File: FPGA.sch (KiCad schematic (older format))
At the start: 1 part, among them U300 LFE5U-12F-8BG256C

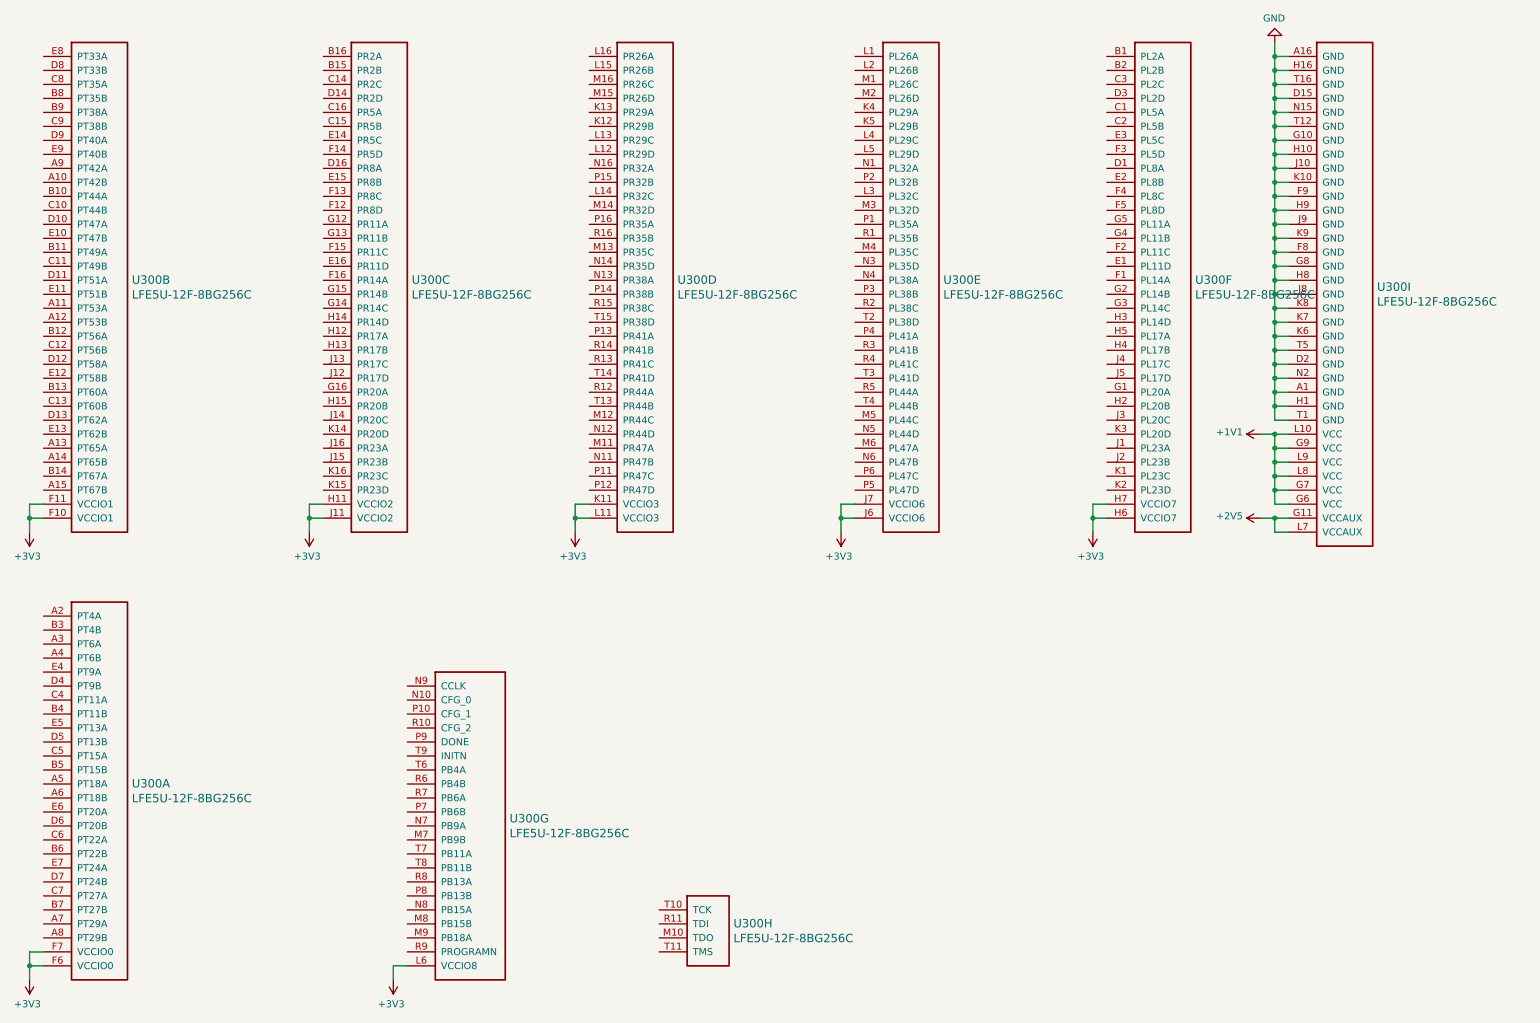
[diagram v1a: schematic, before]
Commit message: updated schematic and initial bga fanout
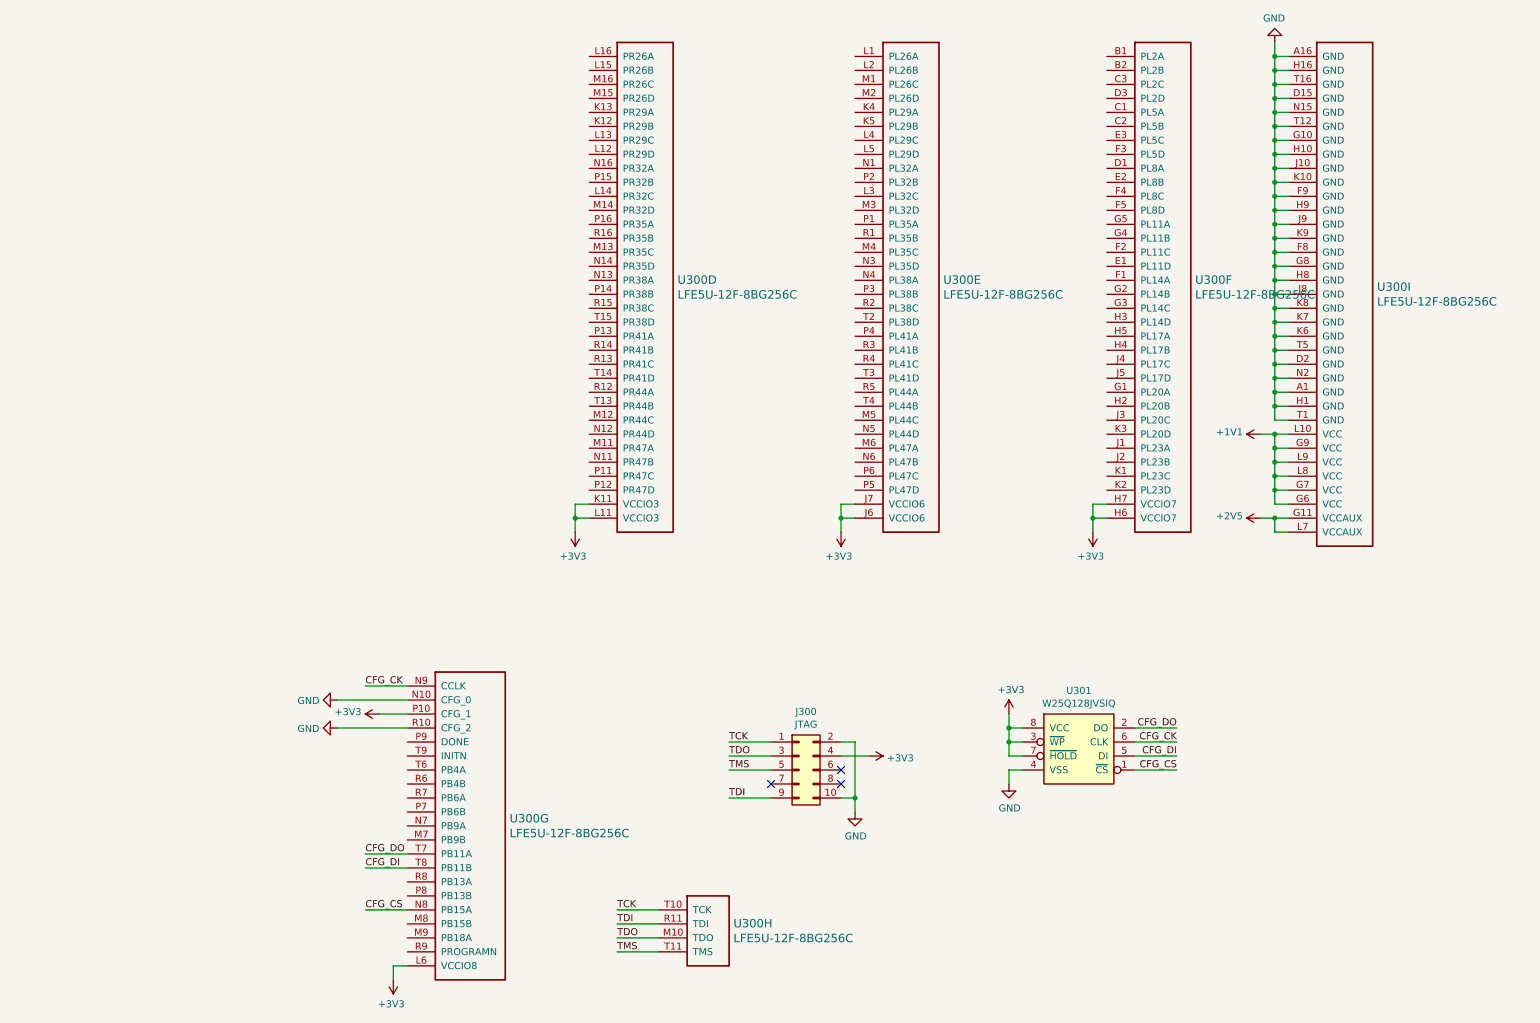
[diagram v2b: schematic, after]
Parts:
- removed unit 1 of U300
- removed unit 2 of U300
- removed unit 3 of U300
- added J300: JTAG, Connector_PinHeader_2.54mm:PinHeader_2x05_P2.54mm_Vertical, symbol Connector_Generic:Conn_02x05_Odd_Even
- added U301: W25Q128JVSIQ, Package_SO:SOIJ-8_5.3x5.3mm_P1.27mm, symbol parts:W25Q128JVSIQ
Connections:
- net +3V3: now also U300.P10 (CFG_1), J300.4 (Pin_4), U301.3 (~WP), U301.7 (~HOLD), U301.8 (VCC)
- net GND: now also U300.N10 (CFG_0), U300.R10 (CFG_2), J300.10 (Pin_10), J300.2 (Pin_2), U301.4 (VSS)
- net CFG_CS: now reaches U300.N8 (PB15A)
- net CFG_CS: now also U301.1 (~CS)
- net CFG_CK: now reaches U300.N9 (CCLK)
- net CFG_CK: now also U301.6 (CLK)
- net CFG_DO: now reaches U300.T7 (PB11A)
- net CFG_DO: now also U301.2 (DO)
- net CFG_DI: now reaches U300.T8 (PB11B)
- net CFG_DI: now also U301.5 (DI)
- net TDO: now reaches U300.M10 (TDO)
- net TDO: now also J300.3 (Pin_3)
- net TDI: now reaches U300.R11 (TDI)
- net TDI: now also J300.9 (Pin_9)
- net TCK: now reaches U300.T10 (TCK)
- net TCK: now also J300.1 (Pin_1)
- net TMS: now reaches U300.T11 (TMS)
- net TMS: now also J300.5 (Pin_5)
- no-connect marks 0 -> 3
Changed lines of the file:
@@
 	5200 4200 5200 4300
-$Comp
-L power:+3V3 #PWR0119
-U 1 1 5C28DDFC
-P 3300 4300
-F 0 "#PWR0119" H 3300 4150 50  0001 C CNN
-F 1 "+3V3" H 3315 4473 50  0000 C CNN
-F 2 "" H 3300 4300 50  0001 C CNN
-F 3 "" H 3300 4300 50  0001 C CNN
-	1    3300 4300
-	-1   0    0    1
-$EndComp
-Wire Wire Line
-	3400 4100 3300 4100
-Wire Wire Line
-	3300 4100 3300 4200
-Wire Wire Line
-	3400 4200 3300 4200
-Connection ~ 3300 4200
-Wire Wire Line
-	3300 4200 3300 4300
-$Comp
-L power:+3V3 #PWR0120
-U 1 1 5C28FB65
-P 1300 4300
-F 0 "#PWR0120" H 1300 4150 50  0001 C CNN
-F 1 "+3V3" H 1315 4473 50  0000 C CNN
-F 2 "" H 1300 4300 50  0001 C CNN
-F 3 "" H 1300 4300 50  0001 C CNN
-	1    1300 4300
-	-1   0    0    1
-$EndComp
-Wire Wire Line
-	1400 4100 1300 4100
-Wire Wire Line
-	1300 4100 1300 4200
-Wire Wire Line
-	1400 4200 1300 4200
-Connection ~ 1300 4200
-Wire Wire Line
-	1300 4200 1300 4300
-$Comp
-L power:+3V3 #PWR0121
-U 1 1 5C291CE2
-P 1300 7500
-F 0 "#PWR0121" H 1300 7350 50  0001 C CNN
-F 1 "+3V3" H 1315 7673 50  0000 C CNN
-F 2 "" H 1300 7500 50  0001 C CNN
-F 3 "" H 1300 7500 50  0001 C CNN
-	1    1300 7500
-	-1   0    0    1
-$EndComp
-Wire Wire Line
-	1400 7300 1300 7300
-Wire Wire Line
-	1300 7300 1300 7400
-Wire Wire Line
-	1400 7400 1300 7400
-Connection ~ 1300 7400
-Wire Wire Line
-	1300 7400 1300 7500
 $Comp
 L power:+3V3 #PWR0122
@@
 $Comp
 L ecp5:LFE5U-12F-8BG256C U300
-U 1 1 5C294BF5
-P 1400 4900
-F 0 "U300" H 2031 3703 60  0000 L CNN
-F 1 "LFE5U-12F-8BG256C" H 2031 3597 60  0000 L CNN
-F 2 "Package_BGA:BGA-256_14.0x14.0mm_Layout16x16_P0.8mm_Ball0.45mm_Pad0.32mm_NSMD" H 1600 4950 60  0001 L CNN
-F 3 "" H 1400 4900 50  0001 C CNN
-	1    1400 4900
-	1    0    0    -1
-$EndComp
-$Comp
-L ecp5:LFE5U-12F-8BG256C U300
-U 2 1 5C294CF4
-P 1400 900
-F 0 "U300" H 2031 -697 60  0000 L CNN
-F 1 "LFE5U-12F-8BG256C" H 2031 -803 60  0000 L CNN
-F 2 "Package_BGA:BGA-256_14.0x14.0mm_Layout16x16_P0.8mm_Ball0.45mm_Pad0.32mm_NSMD" H 1600 950 60  0001 L CNN
-F 3 "" H 1400 900 50  0001 C CNN
-	2    1400 900
-	1    0    0    -1
-$EndComp
-$Comp
-L ecp5:LFE5U-12F-8BG256C U300
-U 3 1 5C294D6A
-P 3400 900
-F 0 "U300" H 4031 -697 60  0000 L CNN
-F 1 "LFE5U-12F-8BG256C" H 4031 -803 60  0000 L CNN
-F 2 "Package_BGA:BGA-256_14.0x14.0mm_Layout16x16_P0.8mm_Ball0.45mm_Pad0.32mm_NSMD" H 3600 950 60  0001 L CNN
-F 3 "" H 3400 900 50  0001 C CNN
-	3    3400 900
-	1    0    0    -1
-$EndComp
-$Comp
-L ecp5:LFE5U-12F-8BG256C U300
 U 4 1 5C294DF3
 P 5300 900
@@
 	1    0    0    -1
 $EndComp
+$Comp
+L parts:W25Q128JVSIQ U301
+U 1 1 5C298D0C
+P 8800 5850
+F 0 "U301" H 8800 6267 50  0000 C CNN
+F 1 "W25Q128JVSIQ" H 8800 6176 50  0000 C CNN
+F 2 "Package_SO:SOIJ-8_5.3x5.3mm_P1.27mm" H 9250 5850 50  0001 C CNN
+F 3 "https://www.micron.com/~/media/documents/products/data-sheet/nor-flash/serial-nor/m25px/m25px32.pdf" H 8950 5750 50  0001 C CNN
+	1    8800 5850
+	1    0    0    -1
+$EndComp
+$Comp
+L power:+3V3 #PWR0123
+U 1 1 5C2999F6
+P 8300 5600
+F 0 "#PWR0123" H 8300 5450 50  0001 C CNN
+F 1 "+3V3" H 8315 5773 50  0000 C CNN
+F 2 "" H 8300 5600 50  0001 C CNN
+F 3 "" H 8300 5600 50  0001 C CNN
+	1    8300 5600
+	1    0    0    -1
+$EndComp
+$Comp
+L power:GND #PWR0124
+U 1 1 5C299A93
+P 8300 6100
+F 0 "#PWR0124" H 8300 5850 50  0001 C CNN
+F 1 "GND" H 8305 5927 50  0000 C CNN
+F 2 "" H 8300 6100 50  0001 C CNN
+F 3 "" H 8300 6100 50  0001 C CNN
+	1    8300 6100
+	1    0    0    -1
+$EndComp
+Wire Wire Line
+	8400 6000 8300 6000
+Wire Wire Line
+	8300 6000 8300 6100
+Wire Wire Line
+	8400 5900 8300 5900
+Wire Wire Line
+	8300 5900 8300 5800
+Wire Wire Line
+	8400 5700 8300 5700
+Connection ~ 8300 5700
+Wire Wire Line
+	8300 5700 8300 5600
+Wire Wire Line
+	8400 5800 8300 5800
+Connection ~ 8300 5800
+Wire Wire Line
+	8300 5800 8300 5700
+Wire Wire Line
+	9500 5700 9200 5700
+Wire Wire Line
+	9500 5800 9200 5800
+Wire Wire Line
+	9500 5900 9200 5900
+Wire Wire Line
+	9500 6000 9200 6000
+Text Label 9500 6000 2    50   ~ 0
+CFG_CS
+Text Label 9500 5700 2    50   ~ 0
+CFG_DO
+Text Label 9500 5800 2    50   ~ 0
+CFG_CK
+Text Label 9500 5900 2    50   ~ 0
+CFG_DI
+$Comp
+L Connector_Generic:Conn_02x05_Odd_Even J300
+U 1 1 5C2A976D
+P 6800 6000
+F 0 "J300" H 6850 6417 50  0000 C CNN
+F 1 "JTAG" H 6850 6326 50  0000 C CNN
+F 2 "Connector_PinHeader_2.54mm:PinHeader_2x05_P2.54mm_Vertical" H 6800 6000 50  0001 C CNN
+F 3 "~" H 6800 6000 50  0001 C CNN
+	1    6800 6000
+	1    0    0    -1
+$EndComp
+Wire Wire Line
+	6300 5800 6600 5800
+Wire Wire Line
+	6300 5900 6600 5900
+Wire Wire Line
+	6300 6000 6600 6000
+Wire Wire Line
+	6300 6200 6600 6200
+NoConn ~ 6600 6100
+NoConn ~ 7100 6100
+NoConn ~ 7100 6000
+$Comp
+L power:GND #PWR0125
+U 1 1 5C2B854B
+P 7200 6300
+F 0 "#PWR0125" H 7200 6050 50  0001 C CNN
+F 1 "GND" H 7205 6127 50  0000 C CNN
+F 2 "" H 7200 6300 50  0001 C CNN
+F 3 "" H 7200 6300 50  0001 C CNN
+	1    7200 6300
+	1    0    0    -1
+$EndComp
+Wire Wire Line
+	7100 6200 7200 6200
+Wire Wire Line
+	7200 6200 7200 6300
+Wire Wire Line
+	7100 5800 7200 5800
+Wire Wire Line
+	7200 5800 7200 6200
+Connection ~ 7200 6200
+$Comp
+L power:+3V3 #PWR0126
+U 1 1 5C2BFE9E
+P 7300 5900
+F 0 "#PWR0126" H 7300 5750 50  0001 C CNN
+F 1 "+3V3" V 7315 6028 50  0000 L CNN
+F 2 "" H 7300 5900 50  0001 C CNN
+F 3 "" H 7300 5900 50  0001 C CNN
+	1    7300 5900
+	0    1    1    0
+$EndComp
+Wire Wire Line
+	7300 5900 7100 5900
+Text Label 6300 5800 0    50   ~ 0
+TCK
+Text Label 6300 5900 0    50   ~ 0
+TDO
+Text Label 6300 6000 0    50   ~ 0
+TMS
+Text Label 6300 6200 0    50   ~ 0
+TDI
+Wire Wire Line
+	5500 7000 5800 7000
+Wire Wire Line
+	5500 7200 5800 7200
+Wire Wire Line
+	5500 7300 5800 7300
+Wire Wire Line
+	5500 7100 5800 7100
+Text Label 5500 7000 0    50   ~ 0
+TCK
+Text Label 5500 7200 0    50   ~ 0
+TDO
+Text Label 5500 7300 0    50   ~ 0
+TMS
+Text Label 5500 7100 0    50   ~ 0
+TDI
+Wire Wire Line
+	3700 6600 4000 6600
+Wire Wire Line
+	3700 5400 4000 5400
+Wire Wire Line
+	3700 6700 4000 6700
+Wire Wire Line
+	3700 7000 4000 7000
+Text Label 3700 7000 0    50   ~ 0
+CFG_CS
+Text Label 3700 6600 0    50   ~ 0
+CFG_DO
+Text Label 3700 5400 0    50   ~ 0
+CFG_CK
+Text Label 3700 6700 0    50   ~ 0
+CFG_DI
+$Comp
+L power:GND #PWR0129
+U 1 1 5C30211A
+P 3500 5500
+F 0 "#PWR0129" H 3500 5250 50  0001 C CNN
+F 1 "GND" V 3505 5372 50  0000 R CNN
+F 2 "" H 3500 5500 50  0001 C CNN
+F 3 "" H 3500 5500 50  0001 C CNN
+	1    3500 5500
+	0    1    1    0
+$EndComp
+$Comp
+L power:+3V3 #PWR0130
+U 1 1 5C3021A7
+P 3800 5600
+F 0 "#PWR0130" H 3800 5450 50  0001 C CNN
+F 1 "+3V3" V 3815 5728 50  0000 L CNN
+F 2 "" H 3800 5600 50  0001 C CNN
+F 3 "" H 3800 5600 50  0001 C CNN
+	1    3800 5600
+	0    -1   -1   0
+$EndComp
+$Comp
+L power:GND #PWR0131
+U 1 1 5C3021F0
+P 3500 5700
+F 0 "#PWR0131" H 3500 5450 50  0001 C CNN
+F 1 "GND" V 3505 5572 50  0000 R CNN
+F 2 "" H 3500 5700 50  0001 C CNN
+F 3 "" H 3500 5700 50  0001 C CNN
+	1    3500 5700
+	0    1    1    0
+$EndComp
+Wire Wire Line
+	3500 5700 4000 5700
+Wire Wire Line
+	3500 5500 4000 5500
+Wire Wire Line
+	4000 5600 3800 5600
 $EndSCHEMATC
